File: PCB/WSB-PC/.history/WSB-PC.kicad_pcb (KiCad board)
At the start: 6 copper layers, 16.5 x 15 mm, 34 parts, among them P2 USB_C_Plug_USB2.0, SW1 SW_SPST_4_PIN, U1 ESP32-C6-MINI-1, U2 74LV1T34, U3 NCP187, U4 TPD2E2U06DRL

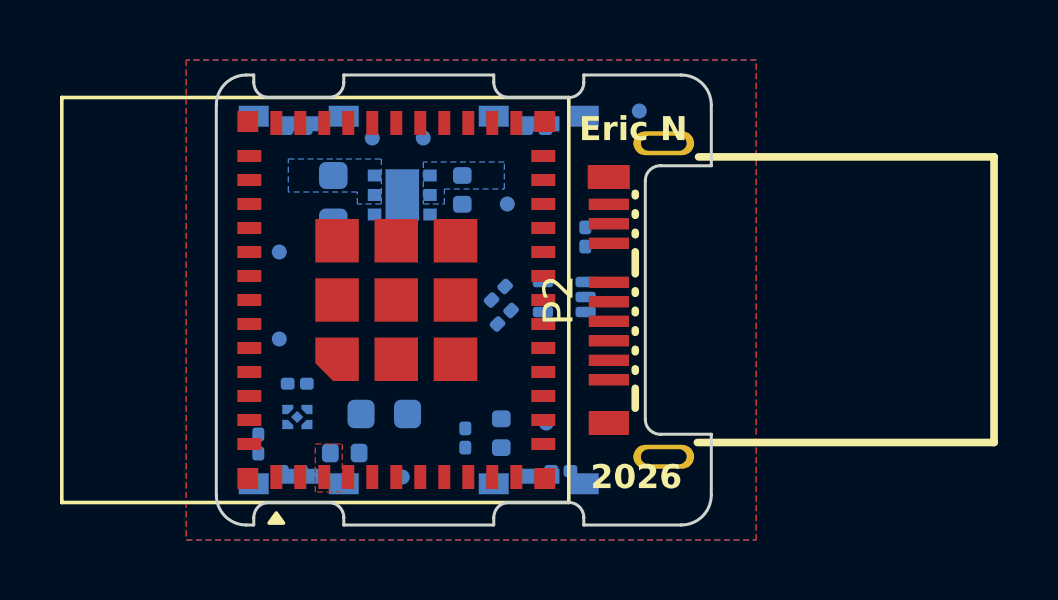
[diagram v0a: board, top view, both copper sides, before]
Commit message: -Changed USB connector -Moved LEDs in behind board edge -Changed to smaller test points
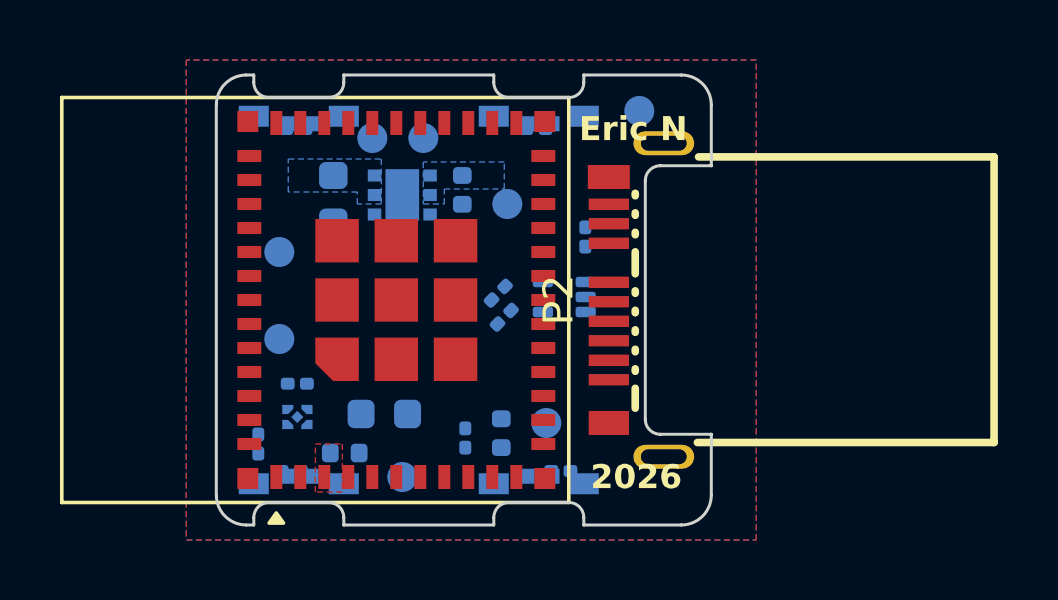
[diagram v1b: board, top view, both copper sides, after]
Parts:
- TP1, TP2, TP3, TP4, TP5, TP6, TP7, TP8: footprint EN_Designs-Footprints:TestPoint_Pad_D0.5mm -> EN_Designs-Footprints:TestPoint_Pad_D1.0mm
- U2: footprint EN_Designs-Footprints:X2SON5_0.8x0.8mm_SOT1226 -> EN_Designs-KiCad-Lib:X2SON5_0.8x0.8mm_SOT1226
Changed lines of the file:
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@@
 		)
 	)
-	(footprint "EN_Designs-Footprints:TestPoint_Pad_D0.5mm"
+	(footprint "EN_Designs-Footprints:TestPoint_Pad_D1.0mm"
 		(layer "B.Cu")
 		(at 129.7 91.8 180)
-		(descr "SMD pad as test Point, diameter 0.5mm")
+		(descr "SMD pad as test Point, diameter 1.0mm")
 		(tags "test point SMD pad")
 		(property "Reference" "TP5"
-			(at 0 1.448 0)
+			(at -0.4 -1.5 0)
 			(layer "B.SilkS")
 			(effects
@@
 		(fp_circle
 			(center 0 0)
-			(end 0.35 0)
+			(end 0 -0.7)
 			(stroke
-				(width 0.1)
+				(width 0.12)
 				(type solid)
 			)
@@
 		(fp_circle
 			(center 0 0)
-			(end 0.25 0)
+			(end 0.6 0)
 			(stroke
 				(width 0.05)
@@
 			(layer "B.CrtYd")
 		)
-		(fp_text user "${REFERENCE}"
-			(at 0 1.45 0)
-			(layer "B.Fab")
-			(effects
-				(font
-					(size 1 1)
-					(thickness 0.15)
-				)
-				(justify mirror)
-			)
-		)
 		(pad "1" smd circle
 			(at 0 0 180)
-			(size 0.5 0.5)
+			(size 1 1)
 			(layers "B.Cu" "B.Mask")
 			(net "/GPIO9")
@@
 		)
 	)
-	(footprint "EN_Designs-Footprints:TestPoint_Pad_D0.5mm"
+	(footprint "EN_Designs-Footprints:TestPoint_Pad_D1.0mm"
 		(layer "B.Cu")
 		(at 125.2 89.6 180)
-		(descr "SMD pad as test Point, diameter 0.5mm")
+		(descr "SMD pad as test Point, diameter 1.0mm")
 		(tags "test point SMD pad")
 		(property "Reference" "TP1"
-			(at 0 1.448 0)
+			(at -1.3 1.3 0)
 			(layer "B.SilkS")
 			(effects
@@
 		(fp_circle
 			(center 0 0)
-			(end 0.35 0)
+			(end 0 -0.7)
 			(stroke
-				(width 0.1)
+				(width 0.12)
 				(type solid)
 			)
@@
 		(fp_circle
 			(center 0 0)
-			(end 0.25 0)
+			(end 0.6 0)
 			(stroke
 				(width 0.05)
@@
 			(layer "B.CrtYd")
 		)
-		(fp_text user "${REFERENCE}"
-			(at 0 1.45 0)
-			(layer "B.Fab")
-			(effects
-				(font
-					(size 1 1)
-					(thickness 0.15)
-				)
-				(justify mirror)
-			)
-		)
 		(pad "1" smd circle
 			(at 0 0 180)
-			(size 0.5 0.5)
+			(size 1 1)
 			(layers "B.Cu" "B.Mask")
 			(net "/ESP_U0_TX")
@@
 		)
 	)
-	(footprint "EN_Designs-Footprints:TestPoint_Pad_D0.5mm"
+	(footprint "EN_Designs-Footprints:TestPoint_Pad_D1.0mm"
 		(layer "B.Cu")
 		(at 122.1 93.4 180)
-		(descr "SMD pad as test Point, diameter 0.5mm")
+		(descr "SMD pad as test Point, diameter 1.0mm")
 		(tags "test point SMD pad")
 		(property "Reference" "TP7"
-			(at 0 1.448 0)
+			(at 0.4 1.4 0)
 			(layer "B.SilkS")
 			(effects
@@
 		(fp_circle
 			(center 0 0)
-			(end 0.35 0)
+			(end 0 -0.7)
 			(stroke
-				(width 0.1)
+				(width 0.12)
 				(type solid)
 			)
@@
 		(fp_circle
 			(center 0 0)
-			(end 0.25 0)
+			(end 0.6 0)
 			(stroke
 				(width 0.05)
@@
 			(layer "B.CrtYd")
 		)
-		(fp_text user "${REFERENCE}"
-			(at 0 1.45 0)
-			(layer "B.Fab")
-			(effects
-				(font
-					(size 1 1)
-					(thickness 0.15)
-				)
-				(justify mirror)
-			)
-		)
 		(pad "1" smd circle
 			(at 0 0 180)
-			(size 0.5 0.5)
+			(size 1 1)
 			(layers "B.Cu" "B.Mask")
 			(net "+3V3")
@@
 		)
 	)
-	(footprint "EN_Designs-Footprints:TestPoint_Pad_D0.5mm"
+	(footprint "EN_Designs-Footprints:TestPoint_Pad_D1.0mm"
 		(layer "B.Cu")
 		(at 126.2 100.9 180)
-		(descr "SMD pad as test Point, diameter 0.5mm")
+		(descr "SMD pad as test Point, diameter 1.0mm")
 		(tags "test point SMD pad")
 		(property "Reference" "TP4"
-			(at 0 1.448 0)
+			(at -2 0 0)
 			(layer "B.SilkS")
 			(effects
@@
 		(fp_circle
 			(center 0 0)
-			(end 0.35 0)
+			(end 0 -0.7)
 			(stroke
-				(width 0.1)
+				(width 0.12)
 				(type solid)
 			)
@@
 		(fp_circle
 			(center 0 0)
-			(end 0.25 0)
+			(end 0.6 0)
 			(stroke
 				(width 0.05)
@@
 			(layer "B.CrtYd")
 		)
-		(fp_text user "${REFERENCE}"
-			(at 0 1.45 0)
-			(layer "B.Fab")
-			(effects
-				(font
-					(size 1 1)
-					(thickness 0.15)
-				)
-				(justify mirror)
-			)
-		)
 		(pad "1" smd circle
 			(at 0 0 180)
-			(size 0.5 0.5)
+			(size 1 1)
 			(layers "B.Cu" "B.Mask")
 			(net "/GPIO3")
@@
 		(embedded_fonts no)
 	)
-	(footprint "EN_Designs-Footprints:TestPoint_Pad_D0.5mm"
+	(footprint "EN_Designs-Footprints:TestPoint_Pad_D1.0mm"
 		(layer "B.Cu")
 		(at 122.1 96.3 180)
-		(descr "SMD pad as test Point, diameter 0.5mm")
+		(descr "SMD pad as test Point, diameter 1.0mm")
 		(tags "test point SMD pad")
 		(property "Reference" "TP6"
-			(at 0 1.448 0)
+			(at 0.1 1.4 0)
 			(layer "B.SilkS")
 			(effects
@@
 		(fp_circle
 			(center 0 0)
-			(end 0.35 0)
+			(end 0 -0.7)
 			(stroke
-				(width 0.1)
+				(width 0.12)
 				(type solid)
 			)
@@
 		(fp_circle
 			(center 0 0)
-			(end 0.25 0)
+			(end 0.6 0)
 			(stroke
 				(width 0.05)
@@
 			(layer "B.CrtYd")
 		)
-		(fp_text user "${REFERENCE}"
-			(at 0 1.45 0)
-			(layer "B.Fab")
-			(effects
-				(font
-					(size 1 1)
-					(thickness 0.15)
-				)
-				(justify mirror)
-			)
-		)
 		(pad "1" smd circle
 			(at 0 0 180)
-			(size 0.5 0.5)
+			(size 1 1)
 			(layers "B.Cu" "B.Mask")
 			(net "+5V")
@@
 		)
 	)
-	(footprint "EN_Designs-Footprints:TestPoint_Pad_D0.5mm"
+	(footprint "EN_Designs-Footprints:TestPoint_Pad_D1.0mm"
 		(layer "B.Cu")
 		(at 126.9 89.6 180)
-		(descr "SMD pad as test Point, diameter 0.5mm")
+		(descr "SMD pad as test Point, diameter 1.0mm")
 		(tags "test point SMD pad")
 		(property "Reference" "TP2"
-			(at 0 1.448 0)
+			(at -2 0.2 0)
 			(layer "B.SilkS")
 			(effects
@@
 		(fp_circle
 			(center 0 0)
-			(end 0.35 0)
+			(end 0 -0.7)
 			(stroke
-				(width 0.1)
+				(width 0.12)
 				(type solid)
 			)
@@
 		(fp_circle
 			(center 0 0)
-			(end 0.25 0)
+			(end 0.6 0)
 			(stroke
 				(width 0.05)
@@
 			(layer "B.CrtYd")
 		)
-		(fp_text user "${REFERENCE}"
-			(at 0 1.45 0)
-			(layer "B.Fab")
-			(effects
-				(font
-					(size 1 1)
-					(thickness 0.15)
-				)
-				(justify mirror)
-			)
-		)
 		(pad "1" smd circle
 			(at 0 0 180)
-			(size 0.5 0.5)
+			(size 1 1)
 			(layers "B.Cu" "B.Mask")
 			(net "/ESP_U0_RX")
@@
 		(embedded_fonts no)
 	)
-	(footprint "EN_Designs-Footprints:TestPoint_Pad_D0.5mm"
+	(footprint "EN_Designs-Footprints:TestPoint_Pad_D1.0mm"
 		(layer "B.Cu")
 		(at 131 99.1 180)
-		(descr "SMD pad as test Point, diameter 0.5mm")
+		(descr "SMD pad as test Point, diameter 1.0mm")
 		(tags "test point SMD pad")
 		(property "Reference" "TP3"
-			(at 0 1.448 0)
+			(at 1.1 1.6 0)
 			(layer "B.SilkS")
 			(effects
@@
 		(fp_circle
 			(center 0 0)
-			(end 0.35 0)
+			(end 0 -0.7)
 			(stroke
-				(width 0.1)
+				(width 0.12)
 				(type solid)
 			)
@@
 		(fp_circle
 			(center 0 0)
-			(end 0.25 0)
+			(end 0.6 0)
 			(stroke
 				(width 0.05)
@@
 			(layer "B.CrtYd")
 		)
-		(fp_text user "${REFERENCE}"
-			(at 0 1.45 0)
-			(layer "B.Fab")
-			(effects
-				(font
-					(size 1 1)
-					(thickness 0.15)
-				)
-				(justify mirror)
-			)
-		)
 		(pad "1" smd circle
 			(at 0 0 180)
-			(size 0.5 0.5)
+			(size 1 1)
 			(layers "B.Cu" "B.Mask")
 			(net "/EN")
@@
 		)
 	)
-	(footprint "EN_Designs-Footprints:TestPoint_Pad_D0.5mm"
+	(footprint "EN_Designs-Footprints:TestPoint_Pad_D1.0mm"
 		(layer "B.Cu")
 		(at 134.1 88.7 180)
-		(descr "SMD pad as test Point, diameter 0.5mm")
+		(descr "SMD pad as test Point, diameter 1.0mm")
 		(tags "test point SMD pad")
 		(property "Reference" "TP8"
-			(at 0 1.448 0)
+			(at -0.1 -1.6 0)
 			(layer "B.SilkS")
 			(effects
@@
 		(fp_circle
 			(center 0 0)
-			(end 0.35 0)
+			(end 0 -0.7)
 			(stroke
-				(width 0.1)
+				(width 0.12)
 				(type solid)
 			)
@@
 		(fp_circle
 			(center 0 0)
-			(end 0.25 0)
+			(end 0.6 0)
 			(stroke
 				(width 0.05)
@@
 			(layer "B.CrtYd")
 		)
-		(fp_text user "${REFERENCE}"
-			(at 0 1.45 0)
-			(layer "B.Fab")
-			(effects
-				(font
-					(size 1 1)
-					(thickness 0.15)
-				)
-				(justify mirror)
-			)
-		)
 		(pad "1" smd circle
 			(at 0 0 180)
-			(size 0.5 0.5)
+			(size 1 1)
 			(layers "B.Cu" "B.Mask")
 			(net "GND")
@@
 		(embedded_fonts no)
 	)
-	(footprint "EN_Designs-Footprints:X2SON5_0.8x0.8mm_SOT1226"
+	(footprint "EN_Designs-KiCad-Lib:X2SON5_0.8x0.8mm_SOT1226"
 		(layer "B.Cu")
 		(at 122.7 98.9 180)
